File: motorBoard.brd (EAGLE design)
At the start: 127 x 76.3 mm, 74 parts

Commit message: save before auto route test
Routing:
- net MOTOR1PWM: track 0.00 -> 62.2 mm, vias 0 -> 1
- net CANTX: track 0.00 -> 37.6 mm, vias 0 -> 4
- net MOTOR3POT: track 0.00 -> 24.8 mm, vias 0 -> 2
- net MOTOR2LIMA: track 0.00 -> 21.0 mm, vias 0 -> 1
- net MOTOR3PWM: track 54.3 -> 52.8 mm, vias 3 -> 2
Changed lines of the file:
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@@
 <contactref element="TCAN" pad="1"/>
 <contactref element="PSOC4200L" pad="14"/>
-<wire x1="85.134" y1="18.781" x2="106.012" y2="30.48" width="0" layer="19" extent="1-1"/>
+<via x="103.913559375" y="25.427559375" extent="1-16" drill="0.35"/>
+<wire x1="106.012" y1="30.48" x2="105.3468" y2="29.8148" width="0.3048" layer="1"/>
+<wire x1="105.3468" y1="29.8148" x2="105.11075" y2="29.8148" width="0.3048" layer="1"/>
+<wire x1="105.11075" y1="29.8148" x2="103.913559375" y2="28.617609375" width="0.3048" layer="1"/>
+<wire x1="103.913559375" y1="28.617609375" x2="103.913559375" y2="25.427559375" width="0.3048" layer="1"/>
+<wire x1="103.913559375" y1="25.427559375" x2="101.572440625" y2="25.427559375" width="0.3048" layer="16"/>
+<wire x1="101.572440625" y1="25.427559375" x2="99.428659375" y2="27.571340625" width="0.3048" layer="16"/>
+<wire x1="99.428659375" y1="27.571340625" x2="99.314" y2="27.686" width="0.3048" layer="16"/>
+<via x="99.428659375" y="27.571340625" extent="1-16" drill="0.35"/>
+<via x="89.789" y="30.099" extent="1-16" drill="0.35"/>
+<wire x1="90.3470875" y1="30.099" x2="89.789" y2="30.099" width="0.3048" layer="1"/>
+<wire x1="90.82038125" y1="29.62570625" x2="90.3470875" y2="30.099" width="0.3048" layer="1"/>
+<wire x1="99.428659375" y1="27.571340625" x2="97.37429375" y2="29.62570625" width="0.3048" layer="1"/>
+<wire x1="97.37429375" y1="29.62570625" x2="90.82038125" y2="29.62570625" width="0.3048" layer="1"/>
+<wire x1="89.789" y1="30.099" x2="84.201" y2="24.511" width="0.3048" layer="16"/>
+<wire x1="84.201" y1="24.511" x2="83.947" y2="24.511" width="0.3048" layer="16"/>
+<wire x1="83.947" y1="24.511" x2="83.058" y2="23.622" width="0.3048" layer="16"/>
+<wire x1="83.058" y1="23.622" x2="82.931" y2="23.622" width="0.3048" layer="16"/>
+<via x="82.931" y="23.622" extent="1-16" drill="0.35"/>
+<wire x1="85.0638" y1="19.50725" x2="85.0638" y2="18.8512" width="0.3048" layer="1"/>
+<wire x1="85.0638" y1="18.8512" x2="85.134" y2="18.781" width="0.3048" layer="1"/>
+<wire x1="82.931" y1="23.622" x2="82.931" y2="21.64005" width="0.3048" layer="1"/>
+<wire x1="82.931" y1="21.64005" x2="85.0638" y2="19.50725" width="0.3048" layer="1"/>
 </signal>
 <signal name="+5V">
@@
 <contactref element="LIMITA2" pad="2"/>
 <contactref element="PSOC4200L" pad="61"/>
-<wire x1="93.584" y1="15.331" x2="106.172" y2="57.785" width="0" layer="19" extent="1-1"/>
+<wire x1="106.172" y1="57.785" x2="106.172" y2="55.88" width="0.3048" layer="1"/>
+<via x="106.172" y="55.88" extent="1-16" drill="0.35"/>
+<wire x1="106.172" y1="55.88" x2="100.965" y2="50.673" width="0.3048" layer="16"/>
+<wire x1="100.965" y1="50.673" x2="100.965" y2="38.989" width="0.3048" layer="16"/>
+<wire x1="93.584" y1="15.331" x2="100.965" y2="38.989" width="0" layer="19" extent="1-16"/>
 </signal>
 <signal name="MOTOR2B3">
@@
 <contactref element="PWM1" pad="2"/>
 <contactref element="PSOC4200L" pad="44"/>
-<wire x1="89.634" y1="7.381" x2="118.872" y2="67.945" width="0" layer="19" extent="1-1"/>
+<wire x1="118.872" y1="67.945" x2="124.587" y2="62.23" width="0.3048" layer="1"/>
+<wire x1="124.587" y1="34.417" x2="123.571" y2="33.401" width="0.3048" layer="1"/>
+<wire x1="123.571" y1="33.401" x2="102.489" y2="33.401" width="0.3048" layer="1"/>
+<wire x1="102.489" y1="33.401" x2="102.362" y2="33.528" width="0.3048" layer="1"/>
+<wire x1="102.362" y1="33.528" x2="99.822" y2="30.988" width="0.3048" layer="1"/>
+<via x="99.822" y="30.988" extent="1-16" drill="0.35"/>
+<wire x1="124.587" y1="62.23" x2="124.587" y2="34.417" width="0.3048" layer="1"/>
+<wire x1="89.634" y1="7.381" x2="99.822" y2="30.988" width="0" layer="19" extent="1-1"/>
 </signal>
 <signal name="MOTOR3A3">
@@
 <contactref element="POT3" pad="2"/>
 <contactref element="PSOC4200L" pad="8"/>
-<wire x1="88.134" y1="18.781" x2="80.772" y2="47.625" width="0" layer="19" extent="1-1"/>
+<wire x1="80.772" y1="47.625" x2="80.772" y2="43.688" width="0.3048" layer="1"/>
+<wire x1="85.979" y1="38.481" x2="86.20795625" y2="27.66095625" width="0.3048" layer="1"/>
+<via x="86.20795625" y="27.66095625" extent="1-16" drill="0.35"/>
+<wire x1="86.20795625" y1="27.66095625" x2="84.41654375" y2="25.69245625" width="0.3048" layer="16"/>
+<via x="84.41654375" y="25.69245625" extent="1-16" drill="0.35"/>
+<wire x1="80.772" y1="43.688" x2="85.979" y2="38.481" width="0.3048" layer="1"/>
+<wire x1="88.134" y1="18.781" x2="84.41654375" y2="25.69245625" width="0" layer="19" extent="1-16"/>
 </signal>
 <signal name="LEVEL_SHIFT_EN3">
@@
 <contactref element="PWM3" pad="2"/>
 <contactref element="PSOC4200L" pad="7"/>
-<wire x1="88.634" y1="18.781" x2="88.5638" y2="18.8512" width="0.3048" layer="1"/>
-<wire x1="88.5638" y1="18.8512" x2="88.5638" y2="19.50725" width="0.3048" layer="1"/>
-<wire x1="85.471" y1="22.60005" x2="85.471" y2="22.733" width="0.3048" layer="1"/>
-<wire x1="88.5638" y1="19.50725" x2="85.471" y2="22.60005" width="0.3048" layer="1"/>
-<via x="85.70579375" y="24.91120625" extent="1-16" drill="0.35"/>
-<wire x1="84.920675" y1="23.0794125" x2="84.5205875" y2="23.4795" width="0.3048" layer="1"/>
-<wire x1="84.5205875" y1="23.4795" x2="84.5205875" y2="24.045325" width="0.3048" layer="1"/>
-<wire x1="84.5205875" y1="24.045325" x2="84.920675" y2="24.4454125" width="0.3048" layer="1"/>
-<wire x1="84.920675" y1="24.4454125" x2="85.24" y2="24.4454125" width="0.3048" layer="1"/>
-<wire x1="85.24" y1="24.4454125" x2="85.70579375" y2="24.91120625" width="0.3048" layer="1"/>
-<wire x1="85.471" y1="22.733" x2="85.1245875" y2="23.0794125" width="0.3048" layer="1"/>
-<wire x1="85.1245875" y1="23.0794125" x2="84.920675" y2="23.0794125" width="0.3048" layer="1"/>
-<wire x1="85.70579375" y1="24.91120625" x2="91.10329375" y2="30.30870625" width="0.3048" layer="16"/>
-<via x="91.10329375" y="30.30870625" extent="1-16" drill="0.35"/>
-<wire x1="91.10329375" y1="30.30870625" x2="95.2942" y2="30.30870625" width="0.3048" layer="1"/>
-<wire x1="95.2942" y1="30.30870625" x2="95.865746875" y2="30.880253125" width="0.3048" layer="1"/>
-<via x="95.865746875" y="30.880253125" extent="1-16" drill="0.35"/>
-<wire x1="95.865746875" y1="30.880253125" x2="100.41849375" y2="35.433" width="0.3048" layer="16"/>
-<wire x1="100.41849375" y1="35.433" x2="111.887" y2="35.433" width="0.3048" layer="16"/>
-<wire x1="111.887" y1="35.433" x2="118.872" y2="42.418" width="0.3048" layer="16"/>
-<wire x1="118.872" y1="42.418" x2="118.872" y2="47.625" width="0.3048" layer="16"/>
+<wire x1="88.88275" y1="17.8762" x2="91.88525" y2="17.8762" width="0.3048" layer="1"/>
+<wire x1="88.634" y1="18.781" x2="88.6768" y2="18.7382" width="0.3048" layer="1"/>
+<wire x1="92.1512" y1="19.7612" x2="93.599" y2="21.209" width="0.3048" layer="1"/>
+<wire x1="88.6768" y1="18.7382" x2="88.6768" y2="18.08215" width="0.3048" layer="1"/>
+<wire x1="88.6768" y1="18.08215" x2="88.88275" y2="17.8762" width="0.3048" layer="1"/>
+<wire x1="91.88525" y1="17.8762" x2="92.1512" y2="18.14215" width="0.3048" layer="1"/>
+<wire x1="92.1512" y1="18.14215" x2="92.1512" y2="19.7612" width="0.3048" layer="1"/>
+<wire x1="93.599" y1="21.209" x2="93.599" y2="26.162" width="0.3048" layer="1"/>
+<via x="93.599" y="26.162" extent="1-16" drill="0.35"/>
+<wire x1="93.599" y1="26.162" x2="101.6" y2="34.163" width="0.3048" layer="16"/>
+<wire x1="101.6" y1="34.163" x2="103.378" y2="34.163" width="0.3048" layer="16"/>
+<via x="103.378" y="34.163" extent="1-16" drill="0.35"/>
+<wire x1="103.378" y1="34.163" x2="104.648" y2="35.433" width="0.3048" layer="1"/>
+<wire x1="117.3988" y1="46.1518" x2="118.872" y2="47.625" width="0.3048" layer="1"/>
+<wire x1="117.3988" y1="36.57675" x2="117.3988" y2="46.1518" width="0.3048" layer="1"/>
+<wire x1="104.648" y1="35.433" x2="116.25505" y2="35.433" width="0.3048" layer="1"/>
+<wire x1="116.25505" y1="35.433" x2="117.3988" y2="36.57675" width="0.3048" layer="1"/>
 </signal>
 <signal name="MOTOR4A3">

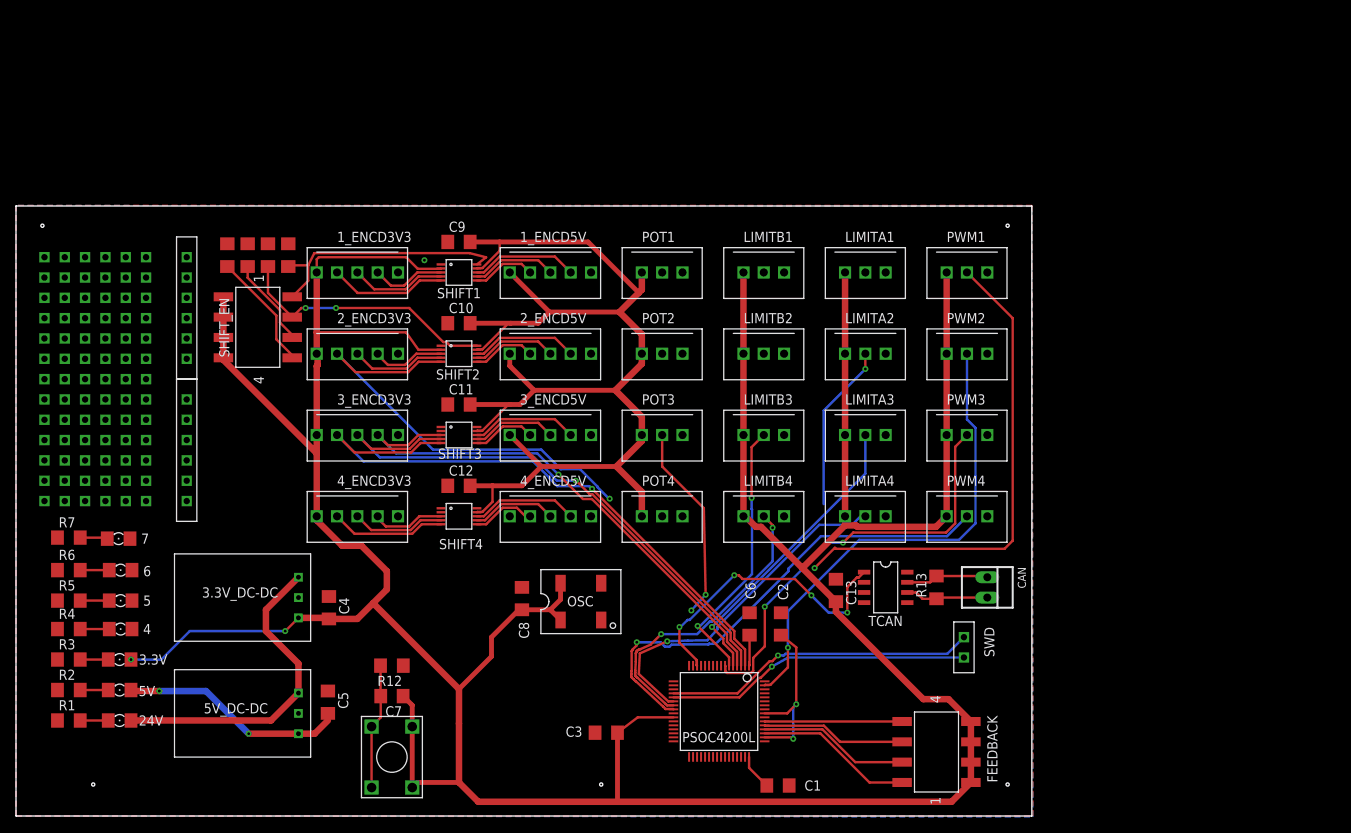
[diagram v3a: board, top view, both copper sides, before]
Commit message: Needs final touches
Used the auto router for some of  the tiny routing around the PSoC which I was struggling with.  TIme for some food and sleep now. Could someone else please finish up the last little trouble shooting?
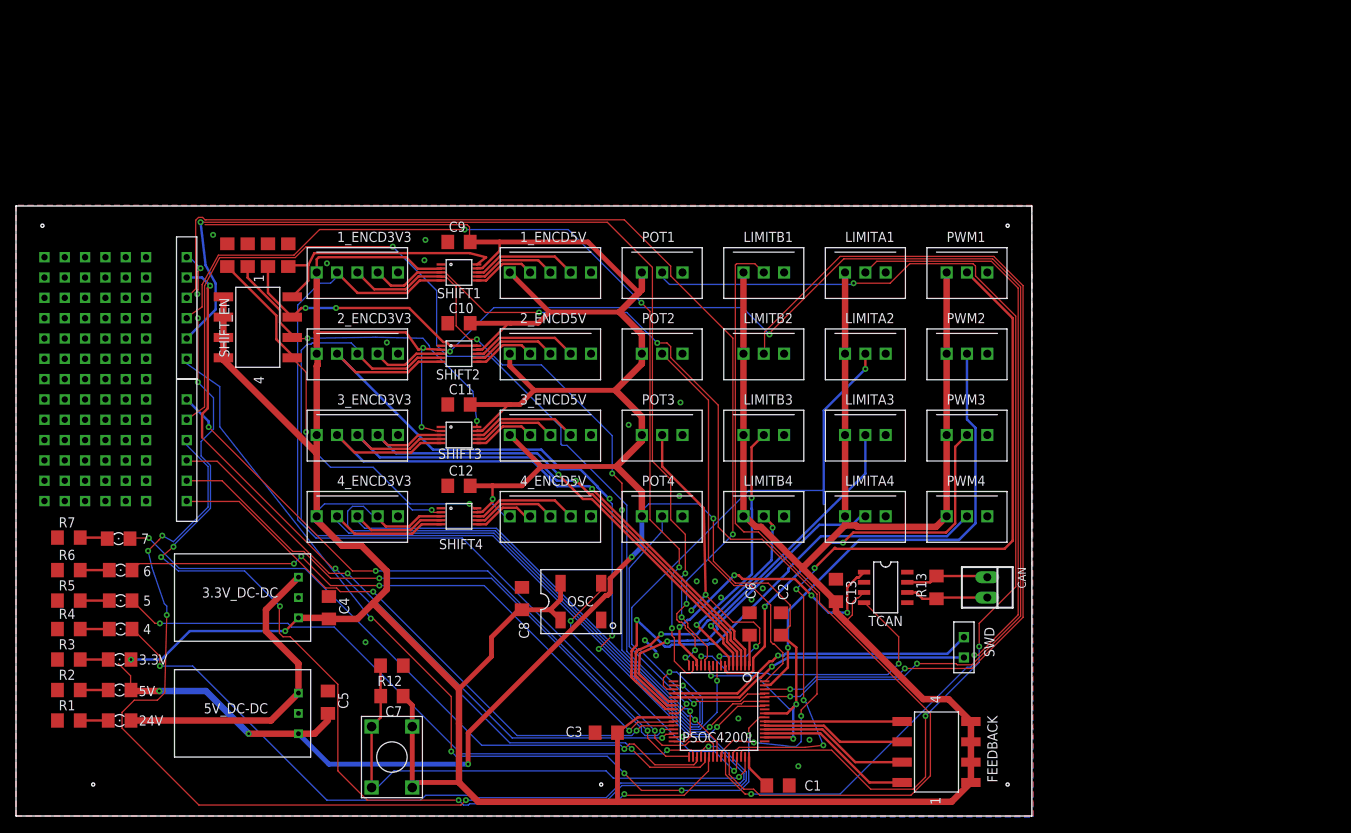
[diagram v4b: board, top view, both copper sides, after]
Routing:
- net MOTOR2A1: track 9.14 -> 168.3 mm, vias 0 -> 4
- net +5V: track 208.6 -> 359.6 mm, vias 4 -> 9
- net BASIC_HEADER1-4: track 0.00 -> 141.6 mm, vias 0 -> 5
- net MOTOR1POT: track 0.00 -> 138.4 mm, vias 0 -> 3
- net BASIC_HEADER2-6: track 0.00 -> 136.8 mm, vias 0 -> 9
- net BASIC_HEADER2-4: track 0.00 -> 130.3 mm, vias 0 -> 4
- net BASIC_HEADER2-2: track 0.00 -> 128.3 mm, vias 0 -> 3
- net BASIC_HEADER1-5: track 0.00 -> 126.9 mm, vias 0 -> 2
- net BASIC_HEADER2-3: track 0.00 -> 118.4 mm, vias 0 -> 4
- net MOTOR2LIMB: track 0.00 -> 118.0 mm, vias 0 -> 2
- net MOTOR1LIMA: track 0.00 -> 111.6 mm, vias 0 -> 2
- net BASIC_HEADER2-1: track 0.00 -> 111.0 mm, vias 0 -> 5
- net MOTOR1LIMB: track 0.00 -> 108.5 mm
- net MOTOR1A1: track 9.28 -> 113.5 mm, vias 0 -> 4
- net BASIC_HEADER2-5: track 0.00 -> 103.6 mm, vias 0 -> 3
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
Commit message: Ground plane tweaks
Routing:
- net +5V: track 359.6 -> 360.3 mm, vias 9 -> 12
- net +3V3: track 484.6 -> 485.1 mm
- net GNDA: vias 18 -> 25
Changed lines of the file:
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@@
 <wire x1="96.972" y1="9.831" x2="97.155" y2="9.648" width="0.3048" layer="1"/>
 <via x="97.155" y="9.648" extent="1-16" drill="0.35"/>
-<wire x1="97.155" y1="9.648" x2="97.155" y2="13.4112" width="0.3048" layer="16"/>
-<wire x1="97.155" y1="13.4112" x2="97.155" y2="13.589" width="0.3048" layer="16"/>
+<wire x1="97.155" y1="9.648" x2="97.155" y2="13.589" width="0.3048" layer="16"/>
 <wire x1="97.155" y1="13.589" x2="97.536" y2="13.97" width="0.3048" layer="16"/>
 <via x="97.536" y="13.97" extent="1-16" drill="0.35"/>
@@
 <wire x1="61.722" y1="37.4904" x2="61.722" y2="37.465" width="0.1524" layer="16"/>
 <wire x1="59.5884" y1="39.624" x2="59.563" y2="39.624" width="0.1524" layer="1"/>
-<wire x1="86.7156" y1="17.6784" x2="86.7156" y2="18.7452" width="0.1524" layer="1"/>
-<wire x1="86.868" y1="17.526" x2="86.7156" y2="17.6784" width="0.1524" layer="1"/>
-<wire x1="92.5068" y1="17.526" x2="86.868" y2="17.526" width="0.1524" layer="16"/>
-<wire x1="96.6216" y1="13.4112" x2="92.5068" y2="17.526" width="0.1524" layer="16"/>
-<wire x1="97.155" y1="13.4112" x2="96.6216" y2="13.4112" width="0.1524" layer="16"/>
-<wire x1="86.7156" y1="18.7452" x2="86.634" y2="18.781" width="0.1524" layer="1"/>
 <wire x1="78.3336" y1="38.2524" x2="78.3336" y2="37.4904" width="0.1524" layer="16"/>
 <wire x1="79.0956" y1="39.0144" x2="78.3336" y2="38.2524" width="0.1524" layer="16"/>
@@
 <wire x1="56.6928" y1="71.9328" x2="56.772" y2="71.755" width="0.1524" layer="1"/>
 <via x="59.5884" y="39.624" extent="1-16" drill="0.35"/>
-<via x="86.868" y="17.526" extent="1-16" drill="0.35"/>
 <via x="87.1728" y="37.1856" extent="1-16" drill="0.35"/>
 <wire x1="78.232" y1="37.465" x2="78.232" y2="33.655" width="0.6096" layer="16"/>
@@
 <wire x1="56.515" y1="6.477" x2="39.116" y2="6.477" width="0.6096" layer="16"/>
 <wire x1="39.116" y1="6.477" x2="35.306" y2="10.287" width="0.6096" layer="16"/>
+<wire x1="86.634" y1="18.781" x2="86.634" y2="18.054" width="0.3048" layer="1"/>
+<wire x1="86.634" y1="18.054" x2="85.852" y2="17.272" width="0.3048" layer="1"/>
+<wire x1="85.852" y1="17.272" x2="85.852" y2="16.256" width="0.3048" layer="1"/>
+<via x="85.852" y="16.256" extent="1-16" drill="0.35"/>
+<wire x1="85.852" y1="16.256" x2="86.614" y2="15.494" width="0.3048" layer="16"/>
+<wire x1="86.614" y1="15.494" x2="86.614" y2="13.081" width="0.3048" layer="16"/>
+<via x="86.614" y="13.081" extent="1-16" drill="0.35"/>
+<wire x1="86.614" y1="13.081" x2="87.81325" y2="13.081" width="0.3048" layer="1"/>
+<wire x1="87.81325" y1="13.081" x2="88.45105" y2="13.7188" width="0.3048" layer="1"/>
+<via x="88.45105" y="13.7188" extent="1-16" drill="0.35"/>
+<wire x1="88.45105" y1="13.7188" x2="90.9292" y2="13.7188" width="0.3048" layer="16"/>
+<wire x1="90.9292" y1="13.7188" x2="91.948" y2="12.7" width="0.3048" layer="16"/>
+<via x="91.948" y="12.7" extent="1-16" drill="0.35"/>
+<wire x1="91.948" y1="12.7" x2="92.583" y2="12.7" width="0.3048" layer="1"/>
+<wire x1="92.714" y1="12.831" x2="93.584" y2="12.831" width="0.3048" layer="1"/>
+<wire x1="92.583" y1="12.7" x2="92.714" y2="12.831" width="0.3048" layer="1"/>
 </signal>
 <signal name="GNDA">
@@
 <wire x1="78.613" y1="21.971" x2="80.01" y2="20.574" width="0.3048" layer="16"/>
 <wire x1="80.01" y1="20.574" x2="80.01" y2="20.066" width="0.3048" layer="16"/>
-<wire x1="82.184" y1="16.831" x2="87.134" y2="18.781" width="0" layer="19" extent="1-1"/>
-<wire x1="102.489" y1="29.594" x2="95.631" y2="25.403" width="0" layer="19" extent="1-1"/>
+<via x="66.421" y="14.605" extent="1-16" drill="0.35"/>
+<via x="25.654" y="3.683" extent="1-16" drill="0.35"/>
+<via x="101.6" y="5.334" extent="1-16" drill="0.35"/>
+<via x="53.34" y="23.241" extent="1-16" drill="0.35"/>
+<via x="121.793" y="35.052" extent="1-16" drill="0.35"/>
+<via x="106.426" y="32.385" extent="1-16" drill="0.35"/>
+<via x="86.868" y="16.891" extent="1-16" drill="0.35"/>
 </signal>
 <signal name="+3V3">
@@
 <wire x1="35.306" y1="24.765" x2="33.655" y2="23.114" width="0.3048" layer="1"/>
 <via x="33.655" y="23.114" extent="1-16" drill="0.35"/>
-<wire x1="33.655" y1="23.114" x2="21.717" y2="23.114" width="0.3048" layer="16"/>
-<wire x1="21.717" y1="23.114" x2="18.161" y2="19.558" width="0.3048" layer="16"/>
-<wire x1="18.161" y1="19.558" x2="14.376" y2="19.558" width="0.3048" layer="16"/>
-<via x="14.376" y="19.558" extent="1-16" drill="0.35"/>
 <wire x1="44.6405" y1="26.6065" x2="55.372" y2="15.875" width="0.8128" layer="1"/>
 <wire x1="55.372" y1="15.875" x2="55.372" y2="11.557" width="0.8128" layer="1"/>
@@
 <via x="50.9016" y="58.5216" extent="1-16" drill="0.35"/>
 <via x="51.9684" y="38.2524" extent="1-16" drill="0.35"/>
+<wire x1="16.51" y1="20.447" x2="16.51" y2="19.558" width="0.3048" layer="16"/>
+<via x="16.51" y="19.558" extent="1-16" drill="0.35"/>
+<wire x1="16.51" y1="19.558" x2="14.376" y2="19.558" width="0.3048" layer="1"/>
+<wire x1="33.655" y1="23.114" x2="19.177" y2="23.114" width="0.3048" layer="16"/>
+<wire x1="19.177" y1="23.114" x2="16.51" y2="20.447" width="0.3048" layer="16"/>
 </signal>
 <signal name="SEL_SW3">
@@
 <wire x1="49.5277625" y1="35.2806" x2="42.3164" y2="35.2806" width="0.3048" layer="1"/>
 <wire x1="42.3164" y1="35.2806" x2="40.132" y2="37.465" width="0.3048" layer="1"/>
-<wire x1="87.63" y1="16.9164" x2="87.63" y2="18.7452" width="0.1524" layer="1"/>
-<wire x1="87.63" y1="12.954" x2="87.63" y2="16.9164" width="0.1524" layer="16"/>
+<wire x1="87.63" y1="16.1544" x2="87.63" y2="18.7452" width="0.1524" layer="1"/>
+<wire x1="87.63" y1="12.954" x2="87.63" y2="16.1544" width="0.1524" layer="16"/>
 <wire x1="85.4964" y1="10.8204" x2="87.63" y2="12.954" width="0.1524" layer="16"/>
 <wire x1="84.2772" y1="10.8204" x2="85.4964" y2="10.8204" width="0.1524" layer="16"/>
@@
 <wire x1="87.63" y1="18.7452" x2="87.634" y2="18.781" width="0.1524" layer="1"/>
 <wire x1="40.2336" y1="37.338" x2="40.132" y2="37.465" width="0.1524" layer="16"/>
-<via x="87.63" y="16.9164" extent="1-16" drill="0.35"/>
+<via x="87.63" y="16.1544" extent="1-16" drill="0.35"/>
 </signal>
 <signal name="MOTOR4A2">
@@
 <via x="90.3732" y="4.8768" extent="1-16" drill="0.35"/>
 </signal>
-<signal name="N$2">
-<via x="88.138" y="27.305" extent="1-16" drill="0.35"/>
-</signal>
 </signals>
